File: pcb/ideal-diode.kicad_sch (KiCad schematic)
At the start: 6 parts, among them Q2 SIS472DN-T1-GE3, U3 LM74700QDBVRQ1

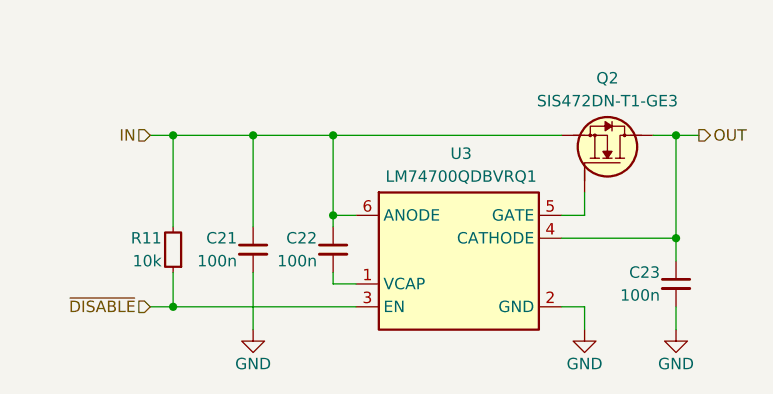
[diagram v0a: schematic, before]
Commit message: [#5] Refactor the schematic
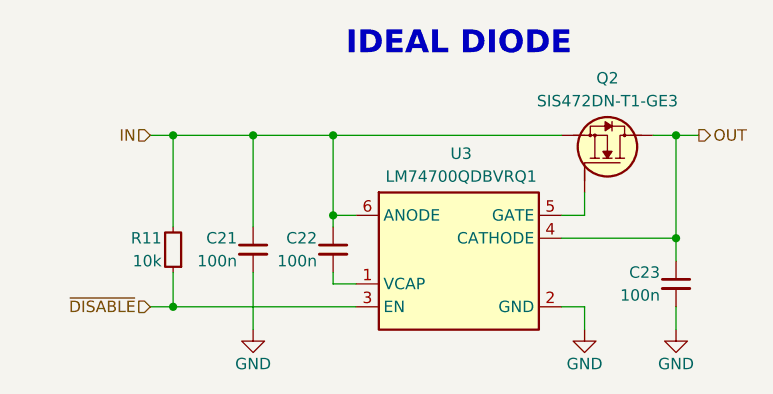
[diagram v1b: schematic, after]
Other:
- note added: "IDEAL DIODE"
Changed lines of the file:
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@@
 		(comment 1 "Project author: Dominik Pluta")
+	)
+	(text "IDEAL DIODE"
+		(exclude_from_sim no)
+		(at 149.86 80.01 0)
+		(effects
+			(font
+				(size 2.54 2.54)
+				(bold yes)
+			)
+		)
 	)
 	(junction
